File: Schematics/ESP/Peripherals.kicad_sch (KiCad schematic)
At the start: 44 parts, among them J12 Battery Input, J3 Battery charger, J4 Motor A, J5 Motor B, J6 Fan, Q17 PJP18N20, SW1 SW_SPDT, U4 DRV8871DDA, U5 LM2596S-5, U6 DRV8871DDA

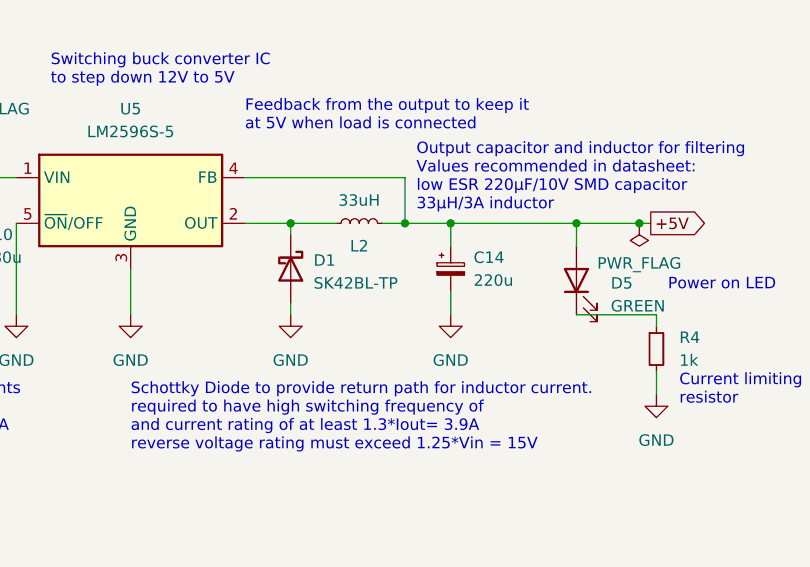
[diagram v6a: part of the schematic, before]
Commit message: changed fuse and regulator output diode
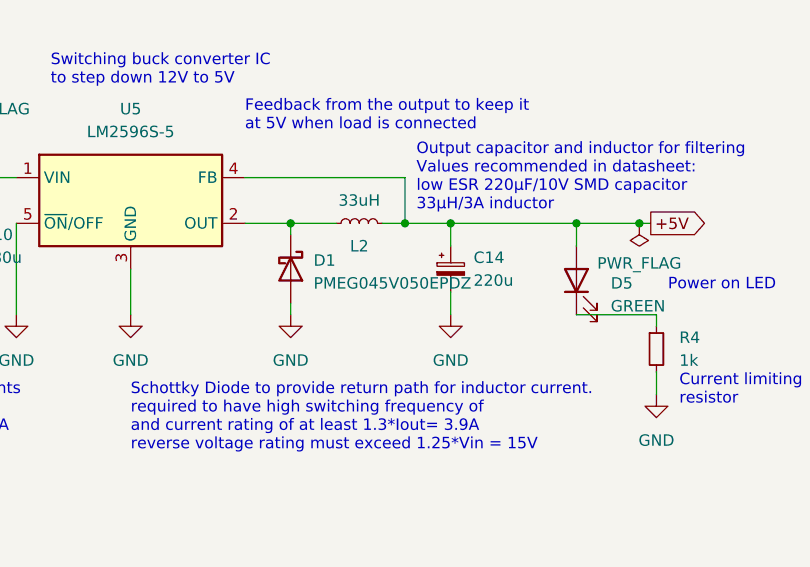
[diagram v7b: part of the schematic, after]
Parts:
- D1: value SK42BL-TP -> PMEG045V050EPDZ; Price 0,52 -> 0,18; digikey link https://www.digikey.fi/en/products/detail/micro-commercial-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 -> https://www.digikey.fi/en/products/detail/rochester-electro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
- F1: Price 0,27 -> 0,39; digikey link https://www.digikey.fi/en/products/detail/bel-fuse-inc/0ZCG0150BF2C/4156109 -> https://www.digikey.fi/en/products/detail/bel-fuse-inc/0ZCG0260BF2B/4156115
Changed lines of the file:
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@@
-    )
-  )
-  (symbol (lib_id "Device:D_Schottky") (at 116.84 59.69 270) (unit 1)
-    (in_bom yes) (on_board yes) (dnp no) (fields_autoplaced)
-    (property "Reference" "D1" (at 119.38 58.7375 90)
-      (effects (font (size 1.27 1.27)) (justify left))
-    )
-    (property "Value" "SK42BL-TP" (at 119.38 61.2775 90)
-      (effects (font (size 1.27 1.27)) (justify left))
-    )
-    (property "Footprint" "Diode_SMD:D_SMB" (at 116.84 59.69 0)
-      (effects (font (size 1.27 1.27)) hide)
-    )
-    (property "Datasheet" "https://www.mccsemi.com/pdf/Products/SK42BL-SK44BL(DO-214AA).pdf" (at 116.84 59.69 0)
-      (effects (font (size 1.27 1.27)) hide)
-    )
-    (property "digikey link" "https://www.digikey.fi/en/products/detail/micro-commercial-co/SK42BL-TP/2642029?s=N4IgTCBcDaIMoGkAsYBCAZAtAFQAogF0BfIA" (at 116.84 59.69 0)
-      (effects (font (size 1.27 1.27)) hide)
-    )
-    (property "Price" "0,52" (at 116.84 59.69 0)
-      (effects (font (size 1.27 1.27)) hide)
-    )
-    (pin "1")
-    (pin "2")
-    (instances
-      (project "ESP"
-        (path "/b616d203-cf5c-462f-b907-860a8573592a/9ad1e8da-d13f-4a6e-8aa2-8655a1d493de"
-          (reference "D1") (unit 1)
-        )
-      )
     )
   )
@@
       (effects (font (size 1.27 1.27)) hide)
     )
-    (property "digikey link" "https://www.digikey.fi/en/products/detail/bel-fuse-inc/0ZCG0150BF2C/4156109" (at 46.99 49.53 90)
-      (effects (font (size 1.27 1.27)) hide)
-    )
-    (property "Price" "0,27" (at 46.99 49.53 0)
+    (property "digikey link" "https://www.digikey.fi/en/products/detail/bel-fuse-inc/0ZCG0260BF2B/4156115" (at 46.99 49.53 90)
+      (effects (font (size 1.27 1.27)) hide)
+    )
+    (property "Price" "0,39" (at 46.99 49.53 0)
       (effects (font (size 1.27 1.27)) hide)
     )
@@
         )
       )
+    )
+  )
+  (symbol (lib_id "Device:D_Schottky") (at 116.84 59.69 270) (unit 1)
+    (in_bom yes) (on_board yes) (dnp no) (fields_autoplaced)
+    (property "Reference" "D1" (at 119.38 58.7375 90)
+      (effects (font (size 1.27 1.27)) (justify left))
+    )
+    (property "Value" "PMEG045V050EPDZ" (at 119.38 61.2775 90)
+      (effects (font (size 1.27 1.27)) (justify left))
+    )
+    (property "Footprint" "Diode_SMD:D_SMB" (at 116.84 59.69 0)
+      (effects (font (size 1.27 1.27)) hide)
+    )
+    (property "Datasheet" "https://assets.nexperia.com/documents/data-sheet/PMEG045V050EPD.pdf" (at 116.84 59.69 0)
+      (effects (font (size 1.27 1.27)) hide)
+    )
+    (property "digikey link" "https://www.digikey.fi/en/products/detail/rochester-electronics-llc/PMEG045V050EPDZ/15637289" (at 116.84 59.69 0)
+      (effects (font (size 1.27 1.27)) hide)
+    )
+    (property "Price" "0,18" (at 116.84 59.69 0)
+      (effects (font (size 1.27 1.27)) hide)
+    )
+    (pin "1")
+    (pin "2")
+    (instances
+      (project "ESP"
+        (path "/b616d203-cf5c-462f-b907-860a8573592a/9ad1e8da-d13f-4a6e-8aa2-8655a1d493de"
+          (reference "D1") (unit 1)
+        )
+      )

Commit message: lots of stuff
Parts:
- removed D5: 1N4001, Diode_THT:D_DO-41_SOD81_P10.16mm_Horizontal, symbol Diode:1N4001
- added D3: PMEG045V050EPDZ, Diode_SMD:D_SMB, symbol Device:D_Schottky
- R3k1, R3k2: value 3k3 -> 3.3
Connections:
- net +12V: now also D3.1 (K)
- net GND: no longer SW1.3 (C)
- net at F1.2, J6.2 (Pin_2): now also D3.2 (A)
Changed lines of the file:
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@@
-    (stroke (width 0) (type default))
-  )
-  (wire (pts (xy 38.1 54.61) (xy 39.37 54.61))
     (stroke (width 0) (type default))
   )
@@
   )
   (wire (pts (xy 197.485 128.905) (xy 197.485 130.81))
-    (stroke (width 0) (type default))
-  )
-  (wire (pts (xy 39.37 54.61) (xy 39.37 63.5))
     (stroke (width 0) (type default))
   )
@@
     )
   )
-  (symbol (lib_id "power:GND") (at 39.37 63.5 0) (unit 1)
-    (in_bom yes) (on_board yes) (dnp no) (fields_autoplaced)
-    (property "Reference" "#PWR010" (at 39.37 69.85 0)
-      (effects (font (size 1.27 1.27)) hide)
-    )
-    (property "Value" "GND" (at 39.37 68.58 0)
-      (effects (font (size 1.27 1.27)))
-    )
-    (property "Footprint" "" (at 39.37 63.5 0)
-      (effects (font (size 1.27 1.27)) hide)
-    )
-    (property "Datasheet" "" (at 39.37 63.5 0)
-      (effects (font (size 1.27 1.27)) hide)
-    )
-    (pin "1")
-    (instances
-      (project "ESP"
-        (path "/b616d203-cf5c-462f-b907-860a8573592a"
-          (reference "#PWR010") (unit 1)
-        )
-        (path "/b616d203-cf5c-462f-b907-860a8573592a/9ad1e8da-d13f-4a6e-8aa2-8655a1d493de"
-          (reference "#PWR02") (unit 1)
-        )
-      )
-    )
-  )
   (symbol (lib_id "Device:D_Schottky") (at 60.96 49.53 180) (unit 1)
     (in_bom yes) (on_board yes) (dnp no) (fields_autoplaced)
@@
       (effects (font (size 1.27 1.27)))
     )
-    (property "Value" "3k3" (at 110.49 152.4 90)
+    (property "Value" "3.3" (at 110.49 152.4 90)
       (effects (font (size 1.27 1.27)))
     )
@@
       (effects (font (size 1.27 1.27)))
     )
-    (property "Value" "3k3" (at 44.45 179.07 90)
+    (property "Value" "3.3" (at 44.45 179.07 90)
       (effects (font (size 1.27 1.27)))
     )
@@
       (effects (font (size 1.27 1.27)))
     )
-    (property "Value" "3k3" (at 95.25 138.43 90)
+    (property "Value" "3.3" (at 95.25 138.43 90)
       (effects (font (size 1.27 1.27)))
     )
@@
     )
   )
+  (symbol (lib_id "Device:D_Schottky") (at 262.89 39.37 270) (unit 1)
+    (in_bom yes) (on_board yes) (dnp no) (fields_autoplaced)
+    (property "Reference" "D3" (at 265.43 38.4175 90)
+      (effects (font (size 1.27 1.27)) (justify left))
+    )
+    (property "Value" "PMEG045V050EPDZ" (at 265.43 40.9575 90)
+      (effects (font (size 1.27 1.27)) (justify left))
+    )
+    (property "Footprint" "Diode_SMD:D_SMB" (at 262.89 39.37 0)
+      (effects (font (size 1.27 1.27)) hide)
+    )
+    (property "Datasheet" "https://assets.nexperia.com/documents/data-sheet/PMEG045V050EPD.pdf" (at 262.89 39.37 0)
+      (effects (font (size 1.27 1.27)) hide)
+    )
+    (property "digikey link" "https://www.digikey.fi/en/products/detail/rochester-electronics-llc/PMEG045V050EPDZ/15637289" (at 262.89 39.37 0)
+      (effects (font (size 1.27 1.27)) hide)
+    )
+    (property "Price" "0,18" (at 262.89 39.37 0)
+      (effects (font (size 1.27 1.27)) hide)
+    )
+    (pin "1")
+    (pin "2")
+    (instances
+      (project "ESP"
+        (path "/b616d203-cf5c-462f-b907-860a8573592a/9ad1e8da-d13f-4a6e-8aa2-8655a1d493de"
+          (reference "D3") (unit 1)
+        )
+      )
+    )
+  )
   (symbol (lib_id "Device:LED") (at 222.25 63.5 90) (unit 1)
     (in_bom yes) (on_board yes) (dnp no) (fields_autoplaced)
@@
       (effects (font (size 1.27 1.27)))
     )
-    (property "Value" "3k3" (at 44.45 167.64 90)
+    (property "Value" "3.3" (at 44.45 167.64 90)
       (effects (font (size 1.27 1.27)))
     )
@@
         )
       )
-    )
-  )
-  (symbol (lib_id "Diode:1N4001") (at 262.89 39.37 270) (unit 1)
-    (in_bom yes) (on_board yes) (dnp no) (fields_autoplaced)
-    (property "Reference" "D5" (at 265.43 38.735 90)
-      (effects (font (size 1.27 1.27)) (justify left))
-    )
-    (property "Value" "1N4001" (at 265.43 41.275 90)
-      (effects (font (size 1.27 1.27)) (justify left))
-    )
-    (property "Footprint" "Diode_THT:D_DO-41_SOD81_P10.16mm_Horizontal" (at 262.89 39.37 0)
-      (effects (font (size 1.27 1.27)) hide)
-    )
-    (property "Datasheet" "http://www.vishay.com/docs/88503/1n4001.pdf" (at 262.89 39.37 0)
-      (effects (font (size 1.27 1.27)) hide)
-    )
-    (property "Sim.Device" "D" (at 262.89 39.37 0)
-      (effects (font (size 1.27 1.27)) hide)
-    )
-    (property "Sim.Pins" "1=K 2=A" (at 262.89 39.37 0)
-      (effects (font (size 1.27 1.27)) hide)
-    )
-    (pin "1")
-    (pin "2")
-    (instances
-      (project "ESP"
-        (path "/b616d203-cf5c-462f-b907-860a8573592a/9ad1e8da-d13f-4a6e-8aa2-8655a1d493de"
-          (reference "D5") (unit 1)
-        )
-      )
